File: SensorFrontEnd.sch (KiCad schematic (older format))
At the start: 7 parts, among them U3 TLC555CD

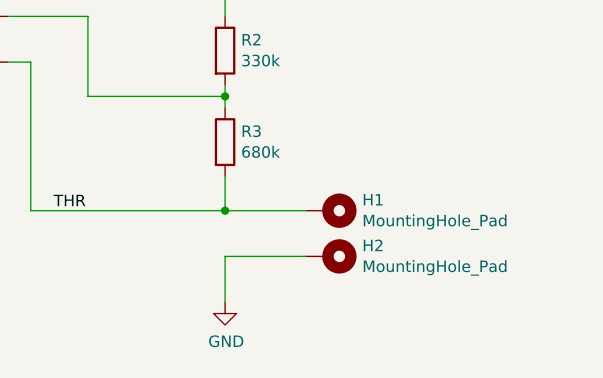
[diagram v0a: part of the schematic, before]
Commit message: added 4-20mA input and PT100 readout
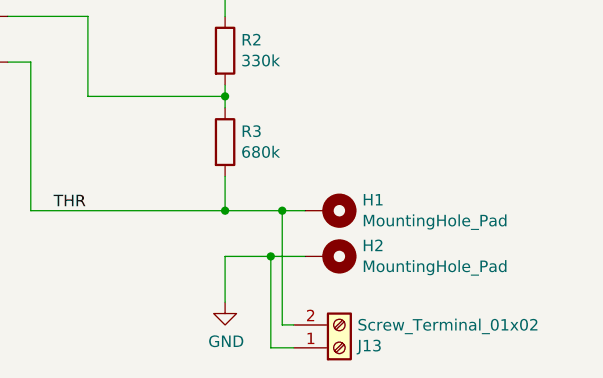
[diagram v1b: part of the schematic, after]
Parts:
- added J13: Screw_Terminal_01x02, TerminalBlock_MetzConnect:TerminalBlock_MetzConnect_Type055_RT01502HDWU_1x02_P5.00mm_Horizontal, symbol Connector:Screw_Terminal_01x02
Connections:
- wire segments 25 -> 31
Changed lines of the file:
@@
 $Descr A4 11693 8268
 encoding utf-8
-Sheet 4 4
+Sheet 3 7
 Title "Capacitive Water Level sensor frontend"
 Date ""
 Rev "1"
-Comp ""
-Comment1 "NE555 based sensor frontend"
+Comp "RWTH Aachen University, Physik 3B"
+Comment1 ""
 Comment2 "convert capacity into frequency"
 Comment3 ""
@@
 	6000 3900 6000 4050
 Wire Wire Line
-	6000 4050 6350 4050
-Wire Wire Line
-	6350 4250 6000 4250
+	6000 4050 6250 4050
+Wire Wire Line
+	6350 4250 6200 4250
 Wire Wire Line
 	6000 4250 6000 4450
@@
 	0    1    1    0
 $EndComp
+$Comp
+L Connector:Screw_Terminal_01x02 J?
+U 1 1 5EEFED68
+P 6500 4650
+AR Path="/5EEFED68" Ref="J?"  Part="1"
+AR Path="/5E78E950/5EEFED68" Ref="J13"  Part="1"
+F 0 "J13" H 6579 4642 50  0000 L CNN
+F 1 "Screw_Terminal_01x02" H 6579 4551 50  0000 L CNN
+F 2 "TerminalBlock_MetzConnect:TerminalBlock_MetzConnect_Type055_RT01502HDWU_1x02_P5.00mm_Horizontal" H 6500 4650 50  0001 C CNN
+F 3 "~" H 6500 4650 50  0001 C CNN
+	1    6500 4650
+	1    0    0    1
+$EndComp
+Wire Wire Line
+	6300 4550 6250 4550
+Wire Wire Line
+	6250 4550 6250 4050
+Connection ~ 6250 4050
+Wire Wire Line
+	6250 4050 6350 4050
+Wire Wire Line
+	6300 4650 6200 4650
+Wire Wire Line
+	6200 4650 6200 4250
+Connection ~ 6200 4250
+Wire Wire Line
+	6200 4250 6000 4250
 $EndSCHEMATC

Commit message: include latest changes
latest changes to design
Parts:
- removed H1, H2: MountingHole_Pad, MountingHole:MountingHole_4.3mm_M4_Pad_Via, symbol Mechanical:MountingHole_Pad
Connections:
- wire segments 31 -> 29
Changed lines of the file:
@@
 EESchema Schematic File Version 4
-LIBS:NodeMCU_WeatherStation-cache
 EELAYER 30 0
 EELAYER END
@@
 	6000 4050 6250 4050
 Wire Wire Line
-	6350 4250 6200 4250
-Wire Wire Line
 	6000 4250 6000 4450
 Wire Wire Line
@@
 	1    6000 2750
 	1    0    0    -1
-$EndComp
-$Comp
-L Mechanical:MountingHole_Pad H1
-U 1 1 5E7B13BD
-P 6450 4050
-F 0 "H1" V 6404 4200 50  0000 L CNN
-F 1 "MountingHole_Pad" V 6495 4200 50  0000 L CNN
-F 2 "MountingHole:MountingHole_4.3mm_M4_Pad_Via" H 6450 4050 50  0001 C CNN
-F 3 "~" H 6450 4050 50  0001 C CNN
-	1    6450 4050
-	0    1    1    0
-$EndComp
-$Comp
-L Mechanical:MountingHole_Pad H2
-U 1 1 5E7B1E5A
-P 6450 4250
-F 0 "H2" V 6404 4400 50  0000 L CNN
-F 1 "MountingHole_Pad" V 6495 4400 50  0000 L CNN
-F 2 "MountingHole:MountingHole_4.3mm_M4_Pad_Via" H 6450 4250 50  0001 C CNN
-F 3 "~" H 6450 4250 50  0001 C CNN
-	1    6450 4250
-	0    1    1    0
 $EndComp
 $Comp
@@
 Wire Wire Line
 	6250 4550 6250 4050
-Connection ~ 6250 4050
-Wire Wire Line
-	6250 4050 6350 4050
 Wire Wire Line
 	6300 4650 6200 4650
 Wire Wire Line
 	6200 4650 6200 4250
-Connection ~ 6200 4250
 Wire Wire Line
 	6200 4250 6000 4250
